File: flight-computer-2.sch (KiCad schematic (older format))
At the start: 6 parts

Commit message: New USB symbol
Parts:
- removed J?: USB4085-GF-A_REVA, GCT_USB4085-GF-A_REVA, symbol flight-computer-2:USB4085-GF-A_REVA
- removed U?: MUN5214DW1T1G, SOT65P210X110-6N, symbol flight-computer-2:MUN5214DW1T1G
- added J?: USB4105-GF-A, GCT_USB4105-GF-A, symbol flight-computer-2:USB4105-GF-A
- added U?: MUN5214DW1T1G, SOT65P210X110-6N, symbol flight-computer-2:MUN5214DW1T1G
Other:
- moved on the sheet: E?, U?
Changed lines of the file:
@@
 L flight-computer-2:ESP32-PICO-D4 U?
 U 1 1 5F12376C
-P 8950 2650
-F 0 "U?" H 8950 4217 50  0000 C CNN
-F 1 "ESP32-PICO-D4" H 8950 4126 50  0000 C CNN
-F 2 "PQFN50P700X700X104-49N" H 8350 1450 50  0001 L BNN
-F 3 "ESP32-PICO-D4" H 8350 1350 50  0001 L BNN
-	1    8950 2650
+P 8600 2650
+F 0 "U?" H 8600 4217 50  0000 C CNN
+F 1 "ESP32-PICO-D4" H 8600 4126 50  0000 C CNN
+F 2 "PQFN50P700X700X104-49N" H 8000 1450 50  0001 L BNN
+F 3 "ESP32-PICO-D4" H 8000 1350 50  0001 L BNN
+	1    8600 2650
 	1    0    0    -1
 $EndComp
@@
 $EndComp
 $Comp
-L flight-computer-2:MUN5214DW1T1G U?
-U 1 1 5F134A8F
-P 2150 7150
-F 0 "U?" H 2150 7520 50  0000 C CNN
-F 1 "MUN5214DW1T1G" H 2150 7429 50  0000 C CNN
-F 2 "SOT65P210X110-6N" H 1800 6750 50  0001 L BNN
-F 3 "SOT65P210X110-6N" H 1800 6850 50  0001 L BNN
-	1    2150 7150
-	1    0    0    -1
-$EndComp
-$Comp
-L flight-computer-2:USB4085-GF-A_REVA J?
-U 1 1 5F135107
-P 1300 5550
-F 0 "J?" H 1243 6417 50  0000 C CNN
-F 1 "USB4085-GF-A_REVA" H 1243 6326 50  0000 C CNN
-F 2 "GCT_USB4085-GF-A_REVA" H 850 4750 50  0001 L BNN
-F 3 "A" H 1250 4650 50  0001 L BNN
-	1    1300 5550
-	-1   0    0    -1
-$EndComp
-$Comp
 L flight-computer-2:PRO-OB-440 E?
 U 1 1 5F136B59
-P 10550 1350
-F 0 "E?" H 10680 1354 50  0000 L CNN
-F 1 "PRO-OB-440" H 10680 1263 50  0000 L CNN
-F 2 "ANT_PRO-OB-440" H 10200 950 50  0001 L BNN
-F 3 "3.2" H 10500 850 50  0001 L BNN
-	1    10550 1350
+P 10200 1350
+F 0 "E?" H 10330 1354 50  0000 L CNN
+F 1 "PRO-OB-440" H 10330 1263 50  0000 L CNN
+F 2 "ANT_PRO-OB-440" H 9850 950 50  0001 L BNN
+F 3 "3.2" H 10150 850 50  0001 L BNN
+	1    10200 1350
 	1    0    0    -1
 $EndComp
@@
 	1    0    0    -1
 $EndComp
+$Comp
+L flight-computer-2:MUN5214DW1T1G U?
+U 1 1 5F13AD1C
+P 2300 6800
+F 0 "U?" H 2300 7167 50  0000 C CNN
+F 1 "MUN5214DW1T1G" H 2300 7076 50  0000 C CNN
+F 2 "SOT65P210X110-6N" H 1950 6400 50  0001 L BNN
+F 3 "SOT65P210X110-6N" H 1950 6500 50  0001 L BNN
+	1    2300 6800
+	1    0    0    -1
+$EndComp
+$Comp
+L flight-computer-2:USB4105-GF-A J?
+U 1 1 5F142775
+P 1600 5300
+F 0 "J?" H 1600 6117 50  0000 C CNN
+F 1 "USB4105-GF-A" H 1600 6026 50  0000 C CNN
+F 2 "GCT_USB4105-GF-A" H 1400 3900 50  0001 L BNN
+F 3 "Package Analog Devices" H 1350 3800 50  0001 L BNN
+	1    1600 5300
+	1    0    0    -1
+$EndComp

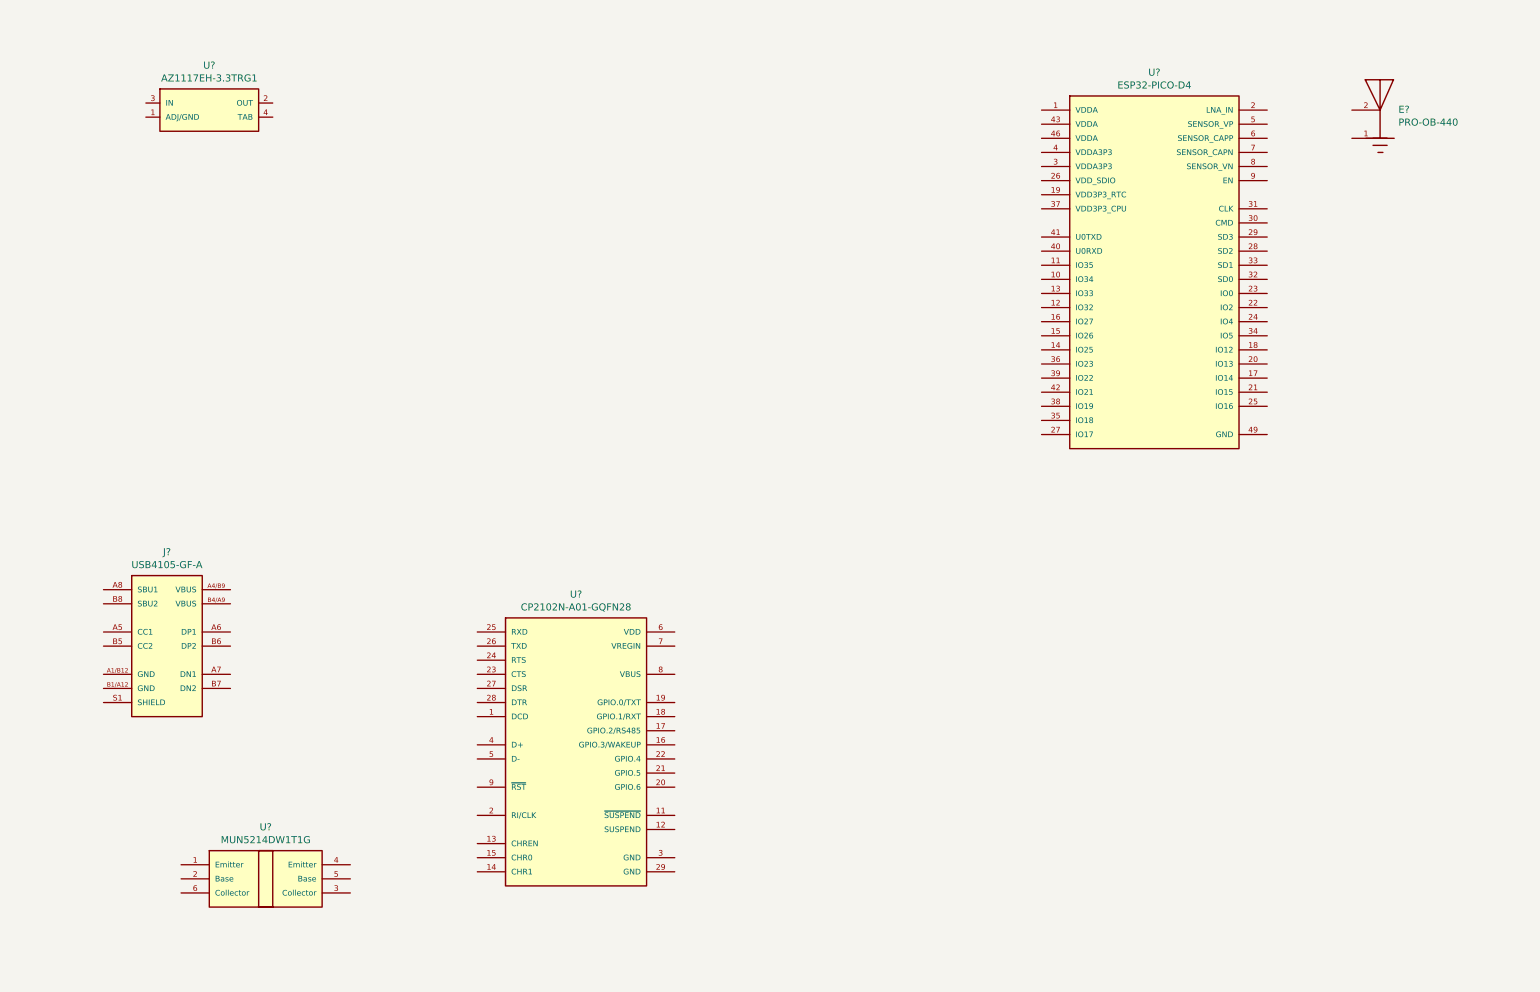
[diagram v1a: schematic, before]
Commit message: Finishing MCU portion of schematic
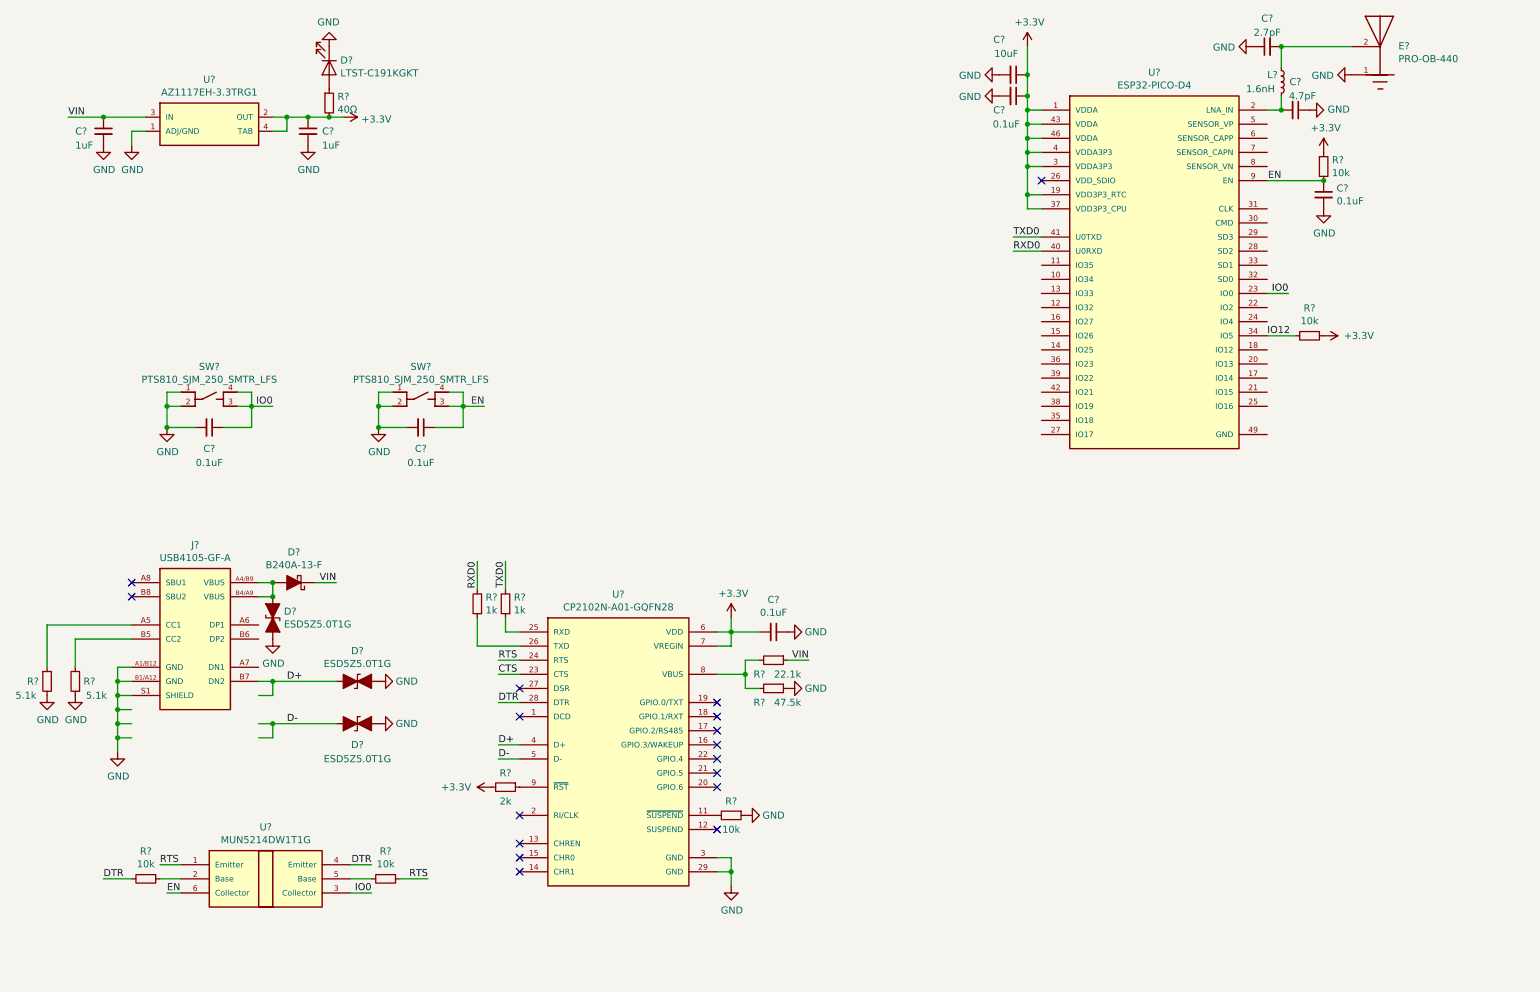
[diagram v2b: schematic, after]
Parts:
- removed J?: USB4105-GF-A, GCT_USB4105-GF-A, symbol flight-computer-2:USB4105-GF-A
- added C? (x2): 1uF, symbol Device:C_Small
- added C? (x5): 0.1uF, symbol Device:C_Small
- added C?: 10uF, symbol Device:C_Small
- added C?: 4.7pF, symbol Device:C_Small
- added C?: 2.7pF, symbol Device:C_Small
- added D? (x3): ESD5Z5.0T1G, symbol Device:D_TVS_ALT
- added D?: B240A-13-F, symbol Device:D_Schottky_ALT
- added D?: LTST-C191KGKT, symbol Device:LED
- added J?: USB4105-GF-A, GCT_USB4105-GF-A, symbol flight-computer-2:USB4105-GF-A
- added L?: 1.6nH, symbol Device:L_Small
- added R?: 40Ω, symbol Device:R_Small
- added R?: 47.5k, symbol Device:R_Small
- added R?: 22.1k, symbol Device:R_Small
- added R? (x5): 10k, symbol Device:R_Small
- added R?: 2k, symbol Device:R_Small
- added R? (x2): 5.1k, symbol Device:R_Small
- added R? (x2): 1k, symbol Device:R_Small
- added SW? (x2): PTS810_SJM_250_SMTR_LFS, SW_PTS810_SJM_250_SMTR_LFS, symbol flight-computer-2:PTS810_SJM_250_SMTR_LFS
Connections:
- net labels added: +3.3V, CTS, D+, D-, DTR, EN, GND, IO0, IO12, RTS, RXD0, TXD0, VIN
- wire segments 0 -> 119
- no-connect marks 0 -> 17
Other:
- moved on the sheet: E?, U?

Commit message: Fixed ERC issues
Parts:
- added D6: LTST-C191KRKT, symbol Device:LED
- added D7: LTST-C191TBKT, symbol Device:LED
- added J2: Conn_01x10, symbol Connector_Generic:Conn_01x10
- added R14, R15: 2k, symbol Device:R_Small
- E1: renamed from E?; footprint ANT_PRO-OB-440 -> (none)
- J1: renamed from J?; footprint GCT_USB4105-GF-A -> (none)
- R4: renamed from R?; value 40Ω -> 2k
- SW1, SW2: renamed from SW?; footprint SW_PTS810_SJM_250_SMTR_LFS -> (none)
- U1: renamed from U?; footprint SOT230P700X180-4N -> (none)
- U2: renamed from U?; footprint SOT65P210X110-6N -> (none)
- U3: renamed from U?; footprint QFN50P500X500X80-29N -> (none)
- U4: renamed from U?; footprint PQFN50P700X700X104-49N -> (none)
- gave numbers to parts that had none: 28
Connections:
- wire segments 119 -> 121
- no-connect marks 17 -> 36
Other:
- moved on the sheet: C1, C10, C2, C3, C6, D1, D2, D3, D4, D5, J1, R1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

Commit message: IMU and barometer circuitry
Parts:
- removed J2: Conn_01x10, symbol Connector_Generic:Conn_01x10
- added C? (x5): 0.1uF, symbol Device:C_Small
- added C? (x2): 22pF, symbol Device:C_Small
- added C?: 1uF, symbol Device:C_Small
- added C?: 10uF, symbol Device:C_Small
- added J?: THR, symbol Connector_Generic:Conn_01x03
- added J?: SER1, symbol Connector_Generic:Conn_01x03
- added J?: SER2, symbol Connector_Generic:Conn_01x03
- added J?: SER3, symbol Connector_Generic:Conn_01x03
- added J?: SER4, symbol Connector_Generic:Conn_01x03
- added J?: EXT, symbol Connector_Generic:Conn_01x03
- added R? (x2): 4.7k, symbol Device:R_Small
- added R? (x5): 10k, symbol Device:R_Small
- added R? (x2): 2.2k, symbol Device:R_Small
- added U?: BNO080, symbol flight-computer-2:BNO080
- added U?: MPL3115A2, symbol flight-computer-2:MPL3115A2
- added Y?: 32.768kHz, symbol Device:Crystal_Small
- renumbered C1 to C?, C2 to C?, C3 to C?, C9 to C?, C6 to C?, C10 to C?, C4 to C?, C5 to C?, C8 to C?, C7 to C?, D5 to D?, D2 to D?, D3 to D?, D4 to D?, D1 to D?, D6 to D?, D7 to D?, E1 to E?, J1 to J?, L1 to L?, R4 to R?, R11 to R?, R9 to R?, R10 to R?, R8 to R?, R1 to R?, R2 to R?, R3 to R?, R5 to R?, R13 to R?, R7 to R?, R6 to R?, R12 to R?, R14 to R?, R15 to R?, SW1 to SW?, SW2 to SW?, U4 to U?, U3 to U?, U1 to U?, U2 to U?
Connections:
- net labels added: ALT_INT_1, ALT_INT_2, IMU_INT, SCL, SDA
- wire segments 121 -> 177
- no-connect marks 36 -> 19
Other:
- moved on the sheet: C?, R?, SW?

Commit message: Servo capacitors
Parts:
- added C2, C3, C4, C5, C6: 470uF, symbol Device:C_Small
- added D1: PMEG10010ELRX, symbol Device:D_Schottky_ALT
- D3: renamed from D?; value B240A-13-F -> PMEG10010ELRX
- gave numbers to parts that had none: 67
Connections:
- net labels added: EXT, SER1, SER2, SER3, SER4, THR
- wire segments 177 -> 189
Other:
- moved on the sheet: C10, C12, C13, C8, C9, J2, J3, J4, J5, J6, J7, R10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

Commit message: Fixed ERC errors
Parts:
- renumbered C1 to C?, C7 to C?, C11 to C?, C23 to C?, C20 to C?, C24 to C?, C17 to C?, C18 to C?, C22 to C?, C21 to C?, C10 to C?, C13 to C?, C12 to C?, C9 to C?, C8 to C?, C19 to C?, C16 to C?, C15 to C?, C14 to C?, C2 to C?, C3 to C?, C4 to C?, C5 to C?, C6 to C?, D6 to D?, D3 to D?, D4 to D?, D5 to D?, D2 to D?, D7 to D?, D8 to D?, D1 to D?, E1 to E?, J1 to J?, J2 to J?, J3 to J?, J4 to J?, J5 to J?, J6 to J?, J7 to J?, L1 to L?, R4 to R?, R18 to R?, R16 to R?, R17 to R?, R12 to R?, R1 to R?, R2 to R?, R3 to R?, R5 to R?, R20 to R?, R11 to R?, R7 to R?, R19 to R?, R21 to R?, R24 to R?, R15 to R?, R14 to R?, R13 to R?, R9 to R?, R10 to R?, R8 to R?, R6 to R?, R22 to R?, R23 to R?, SW1 to SW?, SW2 to SW?, U6 to U?, U4 to U?, U1 to U?, U2 to U?, U3 to U?, U5 to U?, Y1 to Y?
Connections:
- wire segments 189 -> 183
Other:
- moved on the sheet: C?, D?, R?, U?

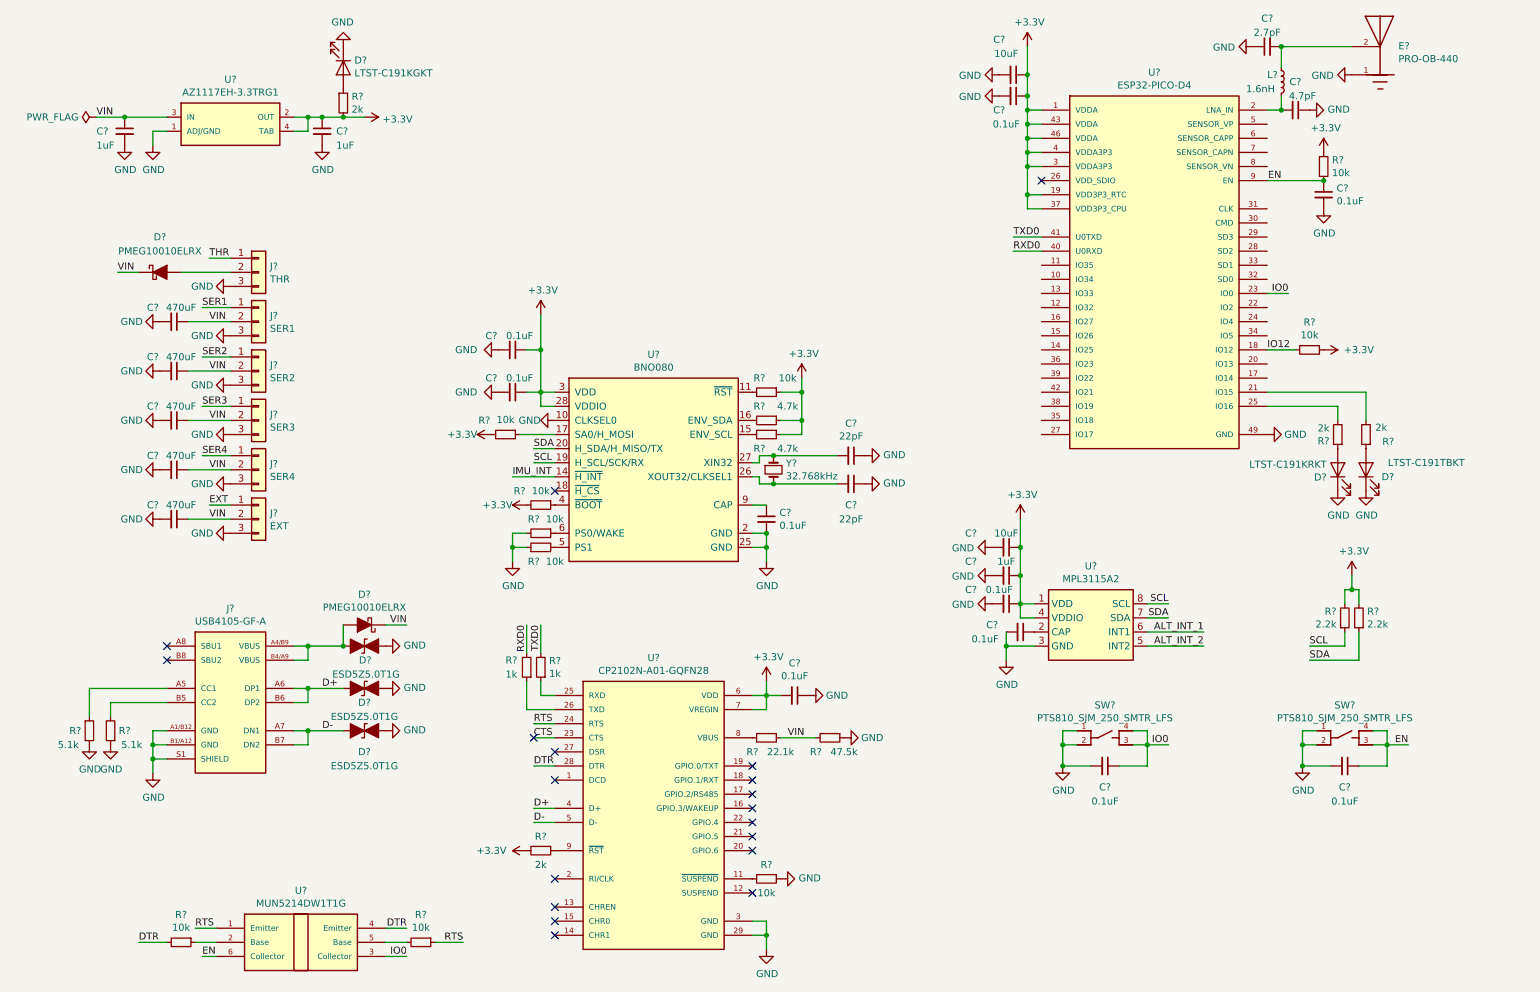
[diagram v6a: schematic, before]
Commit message: Labels and USB/UART bridge correction
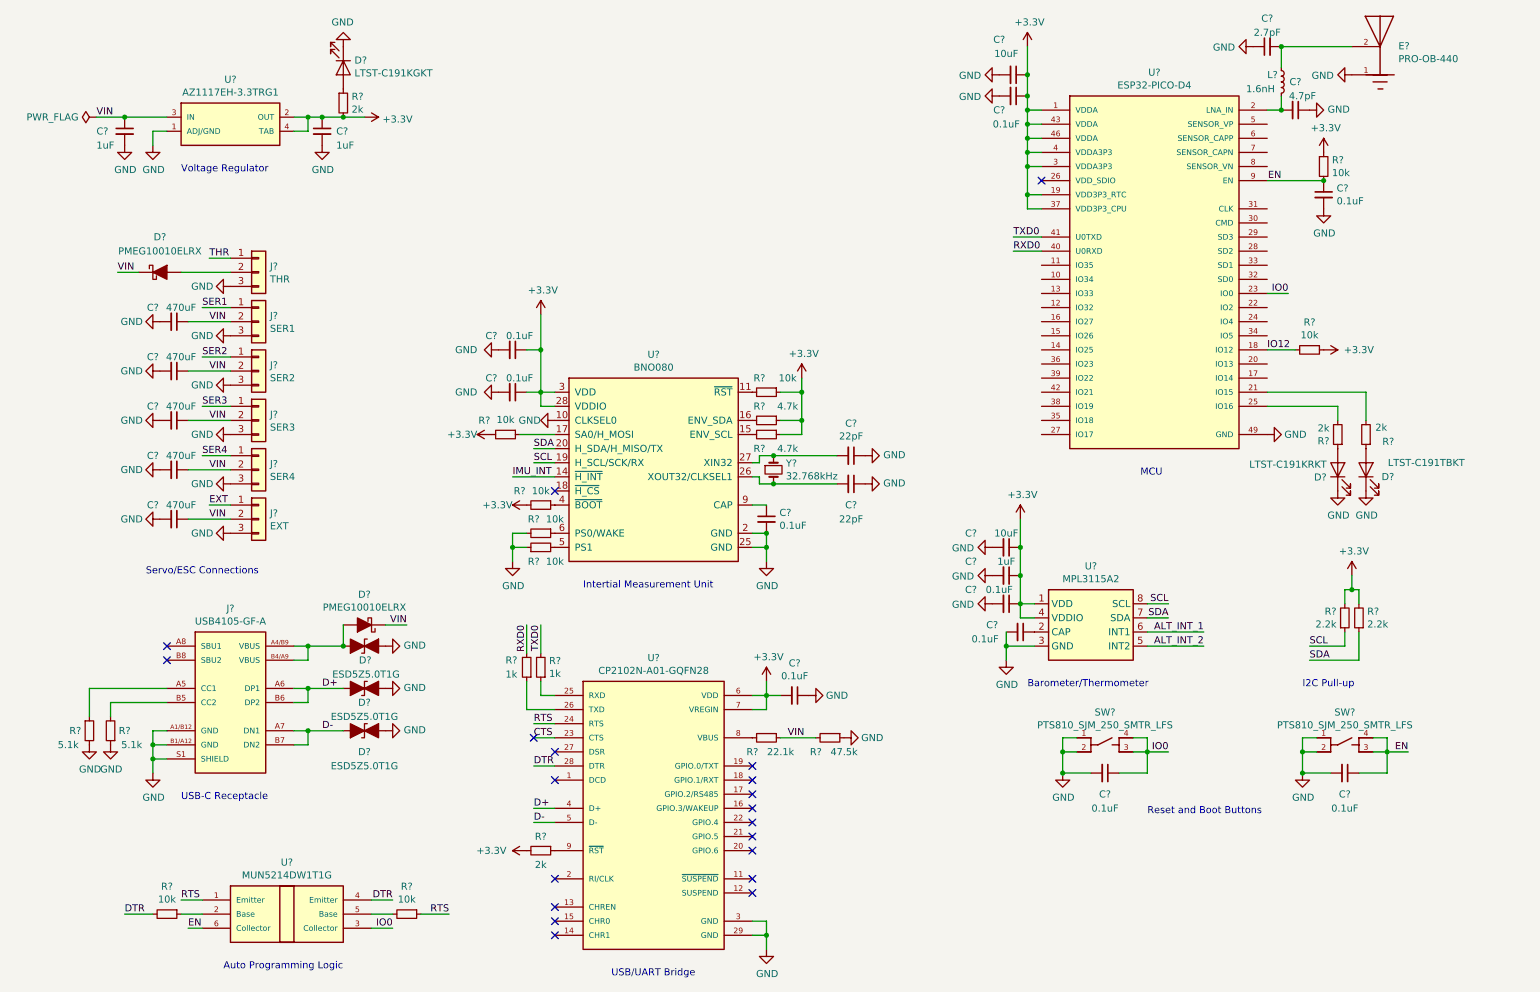
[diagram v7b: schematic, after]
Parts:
- removed R?: 10k, symbol Device:R_Small
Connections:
- no-connect marks 19 -> 20
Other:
- note added: "Auto Programming Logic"
- note added: "Barometer/Thermometer"
- note added: "I2C Pull-up"
- note added: "Intertial Measurement Unit"
- note added: "MCU"
- note added: "Reset and Boot Buttons"
- note added: "Servo/ESC Connections"
- note added: "USB-C Receptacle"
- note added: "USB/UART Bridge"
- note added: "Voltage Regulator"
- moved on the sheet: C?, R?, SW?, U?
